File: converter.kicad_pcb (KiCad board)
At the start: 2 copper layers, 26.4 x 49.9 mm, 69 parts, among them CN1 MINI_DIN_8P_JACK, J1 USB_B, J2 USB_microB, SW1 SW_PUSH, U1 ATMEGA32U4, X1 16MHz

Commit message: Initial commit of PCB rev.2
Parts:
- removed 1, 2, 3, 4, 5, 6, 7, 8, AREF, B0, B1, B2, B3, B4, B5, B6, B7, C7, D+, D-, D0, D2, D3, D4, D5, D6, D7, E6, F0, F1, F4, F5, F6, F7, GND (x3), RST, VCC (x2): CONN_1, PIN_1
- removed the C6 at (136.0, 100.3)
- removed the C6 at (148.7, 97.0)
- removed C7, C8: 0.1u, SM0603_Capa
- removed the D1 at (154.9, 97.3)
- removed the D1 at (141.1, 95.2)
- removed the HOLE_M2.6 at (157.2, 124.6)
- removed the HOLE_M2.6 at (137.7, 85.9)
- removed the HOLE_M2.6 at (157.2, 85.9)
- removed the HOLE_M2.6 at (137.7, 124.6)
- removed J2: USB_microB, USB_microB
- removed R5, R6, R7, R8: 1K, SM0603
- added C6: 22p, 000NewKeyboard_parts:C_1608, F.Cu at (122.4, 122.6)
- added D1: LED, 000NewKeyboard_parts:LED_0805, F.Cu at (101.7, 102.9)
- added HOLE_M2.6: VAL**, HOLE_M2.6, F.Cu at (123.0, 134.0)
- added HOLE_M2.6: VAL**, HOLE_M2.6, F.Cu at (103.4, 107.7)
- added HOLE_M2.6: VAL**, HOLE_M2.6, F.Cu at (122.9, 107.7)
- added HOLE_M2.6: VAL**, HOLE_M2.6, F.Cu at (103.5, 134.0)
- added P1: CONN_1, 000NewKeyboard_parts:PIN_1, F.Cu at (116.8, 130.3)
- added P2: CONN_1, 000NewKeyboard_parts:PIN_1, F.Cu at (114.3, 130.3)
- added P3: CONN_1, 000NewKeyboard_parts:PIN_1, F.Cu at (111.7, 130.3)
- added P4: CONN_1, 000NewKeyboard_parts:PIN_1, F.Cu at (109.2, 130.3)
- added R10: 1K, 000NewKeyboard_parts:R_1608, F.Cu at (122.3, 119.7)
- added R11: 1K, 000NewKeyboard_parts:R_1608, F.Cu at (120.7, 117.7)
- added R12: 1K, 000NewKeyboard_parts:R_1608, F.Cu at (122.3, 115.8)
- added R13: 1K, 000NewKeyboard_parts:R_1608, F.Cu at (120.7, 113.8)
- added R14: 1K, 000NewKeyboard_parts:R_1608, F.Cu at (122.3, 111.8)
- added SJ1: SOLDER_JUMPER, 000NewKeyboard_parts:SOLDER_JUMPER_2, B.Cu at (102.6, 112.7)
- added SJ10: SOLDER_JUMPER, 000NewKeyboard_parts:SOLDER_JUMPER_2, B.Cu at (108.6, 118.7)
- added SJ11: SOLDER_JUMPER, 000NewKeyboard_parts:SOLDER_JUMPER_2, B.Cu at (108.6, 121.7)
- added SJ12: SOLDER_JUMPER, 000NewKeyboard_parts:SOLDER_JUMPER_2, B.Cu at (108.6, 124.7)
- added SJ13: SOLDER_JUMPER, 000NewKeyboard_parts:SOLDER_JUMPER_2, B.Cu at (108.6, 127.7)
- added SJ14: SOLDER_JUMPER, 000NewKeyboard_parts:SOLDER_JUMPER_2, B.Cu at (111.6, 115.7)
- added SJ15: SOLDER_JUMPER, 000NewKeyboard_parts:SOLDER_JUMPER_2, B.Cu at (114.6, 112.7)
- added SJ16: SOLDER_JUMPER, 000NewKeyboard_parts:SOLDER_JUMPER_2, B.Cu at (114.6, 115.7)
- added SJ17: SOLDER_JUMPER, 000NewKeyboard_parts:SOLDER_JUMPER_2, B.Cu at (114.6, 118.7)
- added SJ18: SOLDER_JUMPER, 000NewKeyboard_parts:SOLDER_JUMPER_2, B.Cu at (114.6, 121.7)
- added SJ19: SOLDER_JUMPER, 000NewKeyboard_parts:SOLDER_JUMPER_2, B.Cu at (114.6, 124.7)
- added SJ2: SOLDER_JUMPER, 000NewKeyboard_parts:SOLDER_JUMPER_2, B.Cu at (102.6, 115.7)
- added SJ20: SOLDER_JUMPER, 000NewKeyboard_parts:SOLDER_JUMPER_2, B.Cu at (114.6, 127.7)
- added SJ21: SOLDER_JUMPER, 000NewKeyboard_parts:SOLDER_JUMPER_2, B.Cu at (117.6, 112.7)
- added SJ22: SOLDER_JUMPER, 000NewKeyboard_parts:SOLDER_JUMPER_2, B.Cu at (117.6, 121.7)
- added SJ23: SOLDER_JUMPER, 000NewKeyboard_parts:SOLDER_JUMPER_2, B.Cu at (117.6, 124.7)
- added SJ24: SOLDER_JUMPER, 000NewKeyboard_parts:SOLDER_JUMPER_2, B.Cu at (117.6, 127.7)
- added SJ25: SOLDER_JUMPER, 000NewKeyboard_parts:SOLDER_JUMPER_2, B.Cu at (120.6, 112.7)
- added SJ26: SOLDER_JUMPER, 000NewKeyboard_parts:SOLDER_JUMPER_2, B.Cu at (123.6, 112.7)
- added SJ27: SOLDER_JUMPER, 000NewKeyboard_parts:SOLDER_JUMPER_2, B.Cu at (123.6, 115.7)
- added SJ28: SOLDER_JUMPER, 000NewKeyboard_parts:SOLDER_JUMPER_2, B.Cu at (123.6, 118.7)
- added SJ29: SOLDER_JUMPER, 000NewKeyboard_parts:SOLDER_JUMPER_2, B.Cu at (123.6, 124.7)
- added SJ3: SOLDER_JUMPER, 000NewKeyboard_parts:SOLDER_JUMPER_2, B.Cu at (102.6, 118.7)
- added SJ30: SOLDER_JUMPER, 000NewKeyboard_parts:SOLDER_JUMPER_2, B.Cu at (123.6, 127.7)
- added SJ4: SOLDER_JUMPER, 000NewKeyboard_parts:SOLDER_JUMPER_2, B.Cu at (102.6, 121.7)
- added SJ5: SOLDER_JUMPER, 000NewKeyboard_parts:SOLDER_JUMPER_2, B.Cu at (102.6, 124.7)
- added SJ6: SOLDER_JUMPER, 000NewKeyboard_parts:SOLDER_JUMPER_2, B.Cu at (105.6, 112.7)
- added SJ7: SOLDER_JUMPER, 000NewKeyboard_parts:SOLDER_JUMPER_2, B.Cu at (105.6, 115.7)
- added SJ8: SOLDER_JUMPER, 000NewKeyboard_parts:SOLDER_JUMPER_2, B.Cu at (108.6, 112.7)
- added SJ9: SOLDER_JUMPER, 000NewKeyboard_parts:SOLDER_JUMPER_2, B.Cu at (108.6, 115.7)
- added SJ98: SOLDER_JUMPER, 000NewKeyboard_parts:SOLDER_JUMPER_2, F.Cu at (107.1, 133.2)
- added SJ99: SOLDER_JUMPER, 000NewKeyboard_parts:SOLDER_JUMPER_2, F.Cu at (123.5, 103.6)
- C1: footprint SM1206POL -> 000NewKeyboard_parts:C_1608
- C2, C3, C5: footprint SM0603_Capa -> 000NewKeyboard_parts:C_1608
- C4: value 22p -> 0.1u; footprint SM0603_Capa -> 000NewKeyboard_parts:C_1608
- J1: value USB_B -> USB_mini_micro_B; footprint USB_miniB -> 000NewKeyboard_parts:USB_microB
- R1, R2, R3, R4: footprint SM0603 -> 000NewKeyboard_parts:R_1608
- SW1: footprint SW_ALPS_SKSG -> 000NewKeyboard_parts:SW_ALPS_SKRP
- U1: value ATMEGA32U4 -> ATMEGA32U2; footprint TQFP44 -> 000NewKeyboard_parts:QFP32
- X1: footprint FA-238 -> 000NewKeyboard_parts:FA-238
- moved SW1 53.2 mm to (103.8, 128.6), turned to 90 degrees
- moved C5 44.2 mm to (122.4, 129.4)
- moved C4 43.1 mm to (115.9, 122.9), turned to 0 degrees
- moved C2 41.8 mm to (108.3, 126.4)
- moved CN1 40.8 mm to (113.0, 102.8)
- moved X1 40.3 mm to (122.4, 126.0), turned to 0 degrees
- moved C3 40.2 mm to (116.8, 119.1), turned to 0 degrees
- moved U1 39.8 mm to (108.5, 118.7), turned to 180 degrees
- moved R3 39.3 mm to (102.5, 113.5), turned to 180 degrees
- moved R4 38.6 mm to (102.5, 111.3), turned to 0 degrees
- moved J1 36.5 mm to (113.0, 135.6)
- moved R2 36.4 mm to (111.7, 127.0)
- moved R1 32.2 mm to (114.3, 127.0)
- moved C1 26.3 mm to (119.3, 131.2), turned to 270 degrees
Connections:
- C2 pad 1: N-0000022 -> Net-(C2-Pad1)
- C4 pad 1: N-0000037 -> +5V
- C5 pad 1: N-0000038 -> Net-(C5-Pad1)
- CN1 pad 9: (no net) -> Net-(CN1-Pad9)
- J1 pad 4: (no net) -> Net-(J1-Pad4)
- J1 pad 6: (no net) -> Net-(J1-Pad6)
- R1 pad 1: N-0000025 -> Net-(R1-Pad1)
- R2 pad 1: N-0000024 -> Net-(R2-Pad1)
- R3 pad 2: N-0000013 -> /PD7
- R4 pad 1: +5V -> Net-(D1-Pad2)
- R4 pad 2: /PD0 -> GND
- SW1 pad 1: GND -> /~RESET
- SW1 pad 2: /~RESET -> GND
- U1 pad 1: /PE6 -> Net-(C5-Pad1)
- U1 pad 10: /PB2 -> /PD4
- U1 pad 11: /PB3 -> /PD5
- U1 pad 12: /PB7 -> /PD6
- U1 pad 13: /~RESET -> /PD7
- U1 pad 14: +5V -> /PB0
- U1 pad 15: GND -> /PB1
- U1 pad 16: N-0000037 -> /PB2
- U1 pad 17: N-0000038 -> /PB3
- U1 pad 18: /PD0 -> /PB4
- U1 pad 19: /PD1 -> /PB5
- U1 pad 2: +5V -> Net-(C6-Pad1)
- U1 pad 20: /PD2 -> /PB6
- U1 pad 21: /PD3 -> /PB7
- U1 pad 22: /PD5 -> /PC7
- U1 pad 23: GND -> /PC6
- U1 pad 24: +5V -> /~RESET
- U1 pad 25: /PD4 -> /PC5
- U1 pad 26: /PD6 -> /PC4
- U1 pad 27: /PD7 -> Net-(C2-Pad1)
- U1 pad 28: /PB4 -> GND
- U1 pad 29: /PB5 -> Net-(R2-Pad1)
- U1 pad 3: N-0000025 -> GND
- U1 pad 30: /PB6 -> Net-(R1-Pad1)
- U1 pad 31: /PC6 -> +5V
- U1 pad 32: /PC7 -> +5V
- U1 pad 4: N-0000024 -> +5V
- U1 pad 5: GND -> /PC2
- U1 pad 6: N-0000022 -> /PD0
- U1 pad 7: +5V -> /PD1
- U1 pad 8: /PB0 -> /PD2
- U1 pad 9: /PB1 -> /PD3
- X1 pad 1: N-0000037 -> Net-(C5-Pad1)
- X1 pad 2: N-0000038 -> Net-(C6-Pad1)
- X1 pad 3: (no net) -> GND
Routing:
- net GND: track 51.3 -> 151.1 mm, vias 12 -> 4
- net /PD4: track 5.77 -> 33.0 mm, vias 1 -> 2
- net /DIN8: track 7.30 -> 32.9 mm, vias 0 -> 1
- net /DIN5: track 8.30 -> 33.6 mm
- net +5V: track 83.0 -> 104.4 mm, vias 0 -> 4
- net /PD0: track 22.0 -> 43.2 mm, vias 1 -> 5
- net /DIN3: track 8.09 -> 28.9 mm
- net /DIN6: track 9.59 -> 30.0 mm, vias 0 -> 1
- net /PB7: track 19.6 -> 0.00 mm
- net /PD1: track 20.1 -> 39.1 mm, vias 1 -> 3
- net /PB6: track 17.4 -> 0.00 mm, vias 1 -> 0
- net /PE6: track 17.3 -> 0.00 mm, vias 1 -> 0
- net Net-(C6-Pad1): track 0.00 -> 16.8 mm
- net /PB4: track 15.7 -> 0.00 mm, vias 1 -> 0
- net Net-(C5-Pad1): track 0.00 -> 14.8 mm
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- added copper zone on F.Cu, net GND
- removed copper zone on F.Cu, net +5V
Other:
- board size 26.4 x 49.9 mm -> 26 x 37 mm
- net class 12tho removed
- net class Default: trace_width 0.2032 -> 0.254; via_dia 0.762 -> 0.889
- net class Min6mil added: clearance 0.1524, trace_width 0.1524, via_dia 0.889, via_drill 0.508
- net class Min8mil added: clearance 0.2032, trace_width 0.2032, via_dia 0.889, via_drill 0.508
- net class Power added: clearance 0.254, trace_width 0.381, via_dia 0.889, via_drill 0.508
- rule trace_min: 0.2032 -> 0.1524
- board text added: "1"
- board text added: "2"
- board text added: "3"
- board text added: "4"
- board text added: "5"
- board text added: "6"
- board text added: "7"
- board text added: "8"
- board text added: "ADB"
- board text added: "NEXT"
- board text added: "PC98"
- board text added: "PS/2"
- board text added: "SUN"
- board text added: "X68K"
- board text removed: "May 2013"
- board text removed: "TMK"
- board text removed: "Tokyo JAPAN"
- board text removed: "keyboard"
- board text removed: "rev.1"

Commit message: Clean library.
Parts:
- R3: value 1k -> 1K
- U1: value ATMEGA32U2 -> 32U2
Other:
- board text added: "+"
- board text added: "-"
- board text added: "D0"
- board text added: "D1"
- board text added: "D2"
- board text added: "D3"
- board text added: "D4"
- board text added: "FG"
- board text added: "G"
- board text added: "HWB"
- board text added: "V"

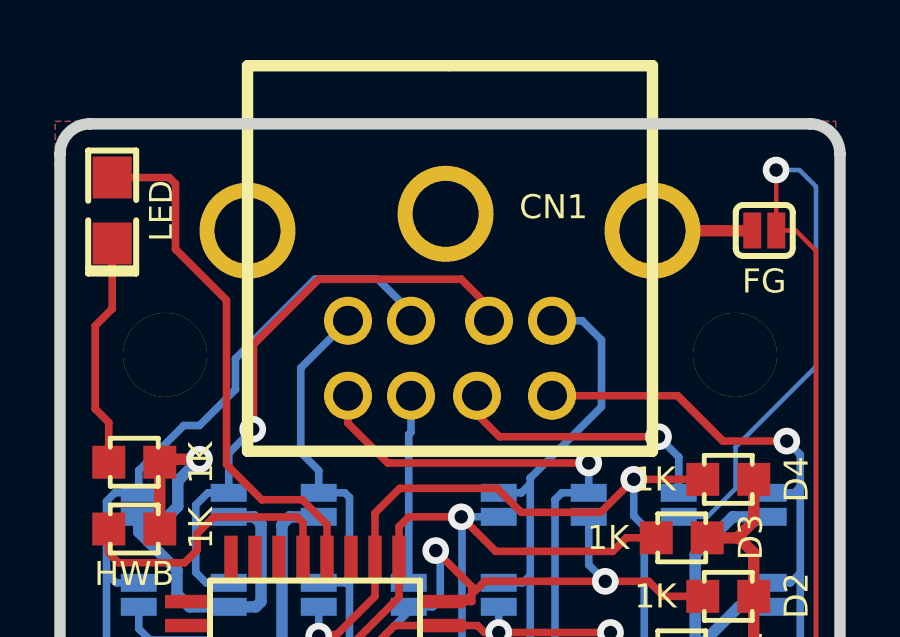
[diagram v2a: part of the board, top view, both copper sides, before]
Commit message: Update Mini DIN module and vix PCB.
- Wrong pad alignment
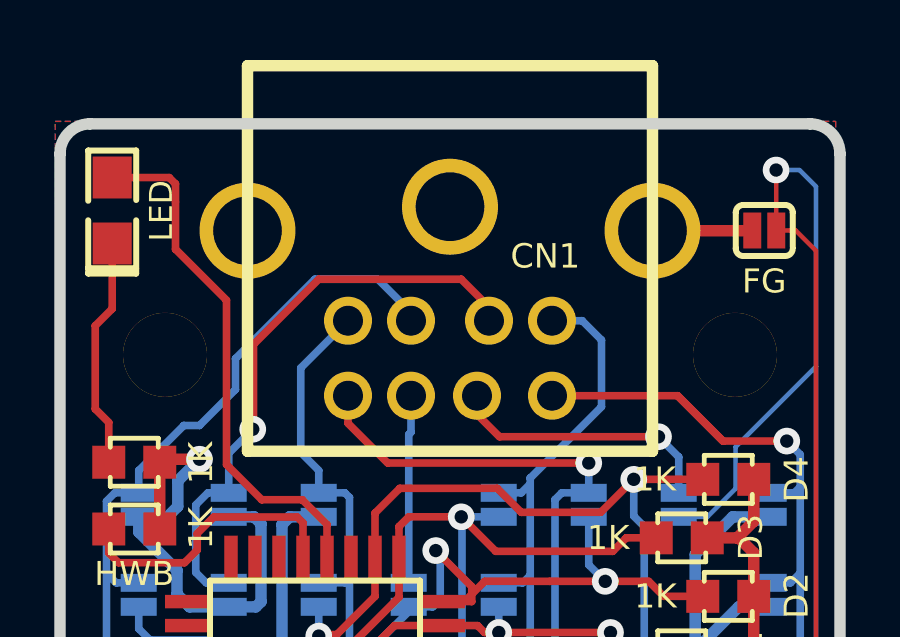
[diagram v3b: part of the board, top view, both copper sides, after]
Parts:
- CN1: footprint MINI_DIN_8 -> 000NewKeyboard_parts:MINI_DIN_8

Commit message: rev2.1
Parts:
- R3: value 1K -> 1k
- R4: value 1K -> R_LED
- U1: value 32U2 -> ATMEGA32U2
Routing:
- net Net-(J1-Pad6): track 4.86 -> 2.43 mm
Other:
- rule pad_to_mask_clearance: 0.254 -> 0.1

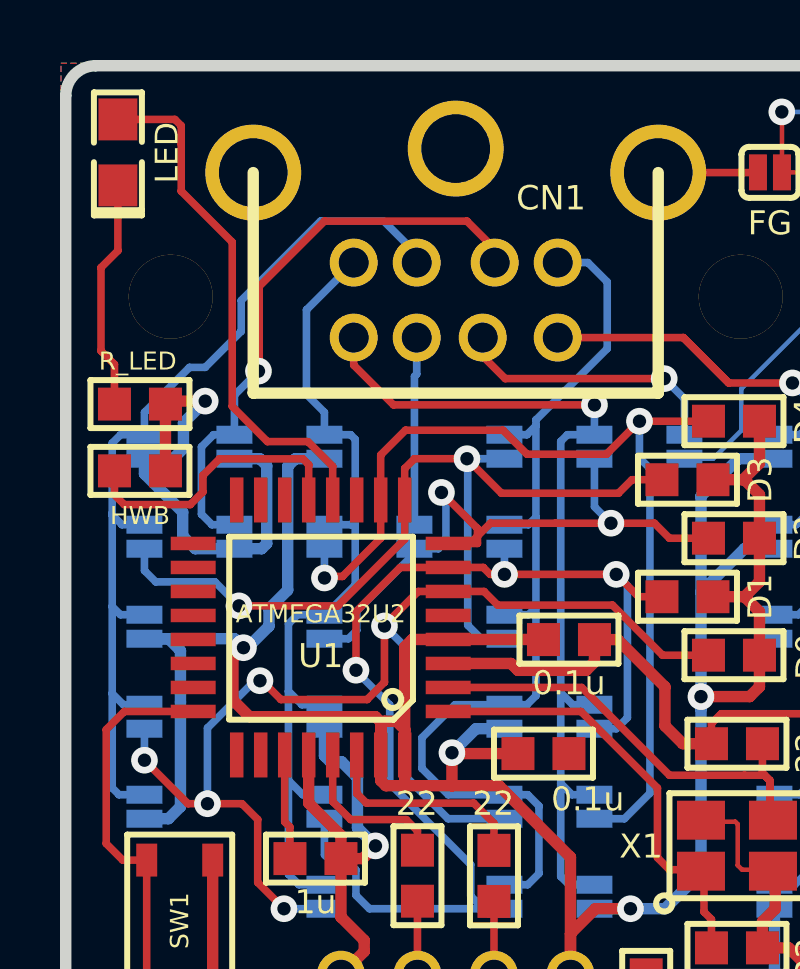
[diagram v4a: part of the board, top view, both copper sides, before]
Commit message: Change LED footprint and add numbering silks
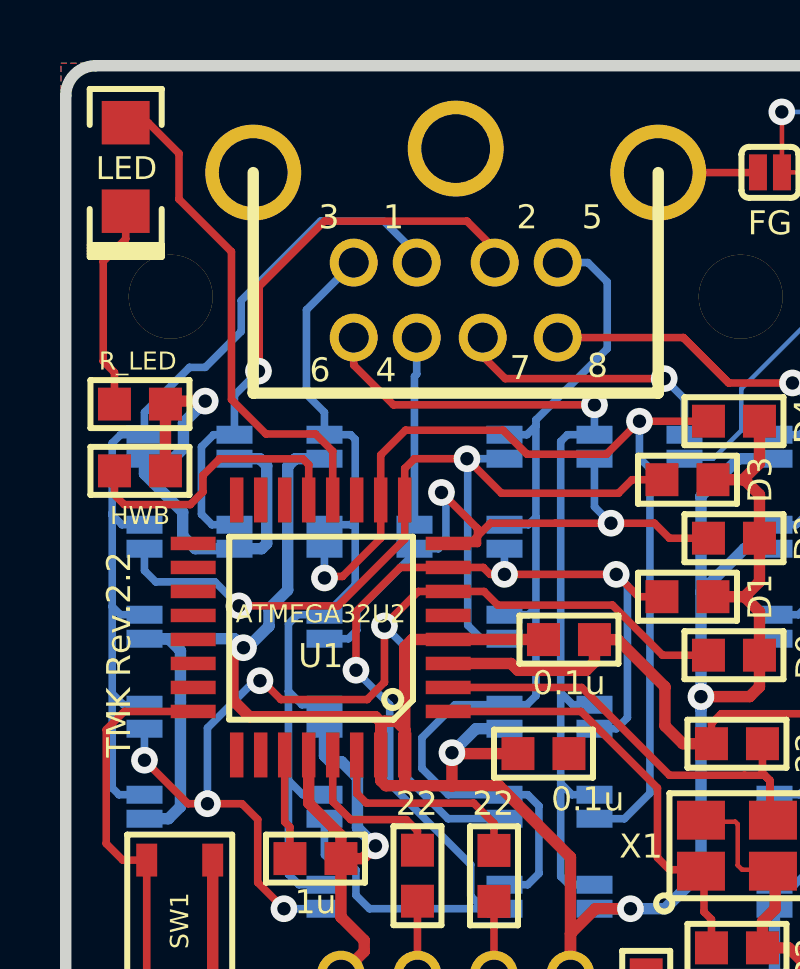
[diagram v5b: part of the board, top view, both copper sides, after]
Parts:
- D1: footprint 000NewKeyboard_parts:LED_0805 -> keyboard_parts:LED_3020_REFLOW
- moved D1 0.55 mm to (102.0, 103.4)
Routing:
- net Net-(D1-Pad2): track 7.71 -> 6.90 mm
- net /PD6: track 17.6 -> 16.8 mm
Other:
- rule pad_to_mask_clearance: 0.1 -> 0.2
- board text added: "TMK Rev.2.2"

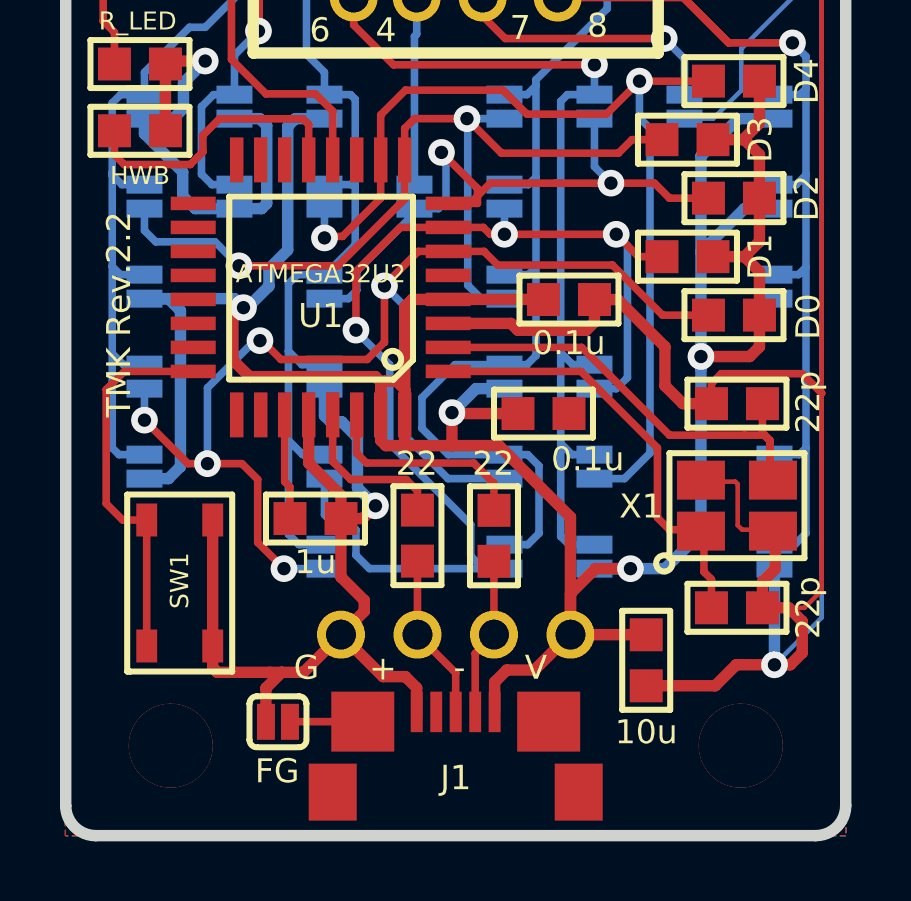
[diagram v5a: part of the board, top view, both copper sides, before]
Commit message: Change values of capacitors and solder mask setting
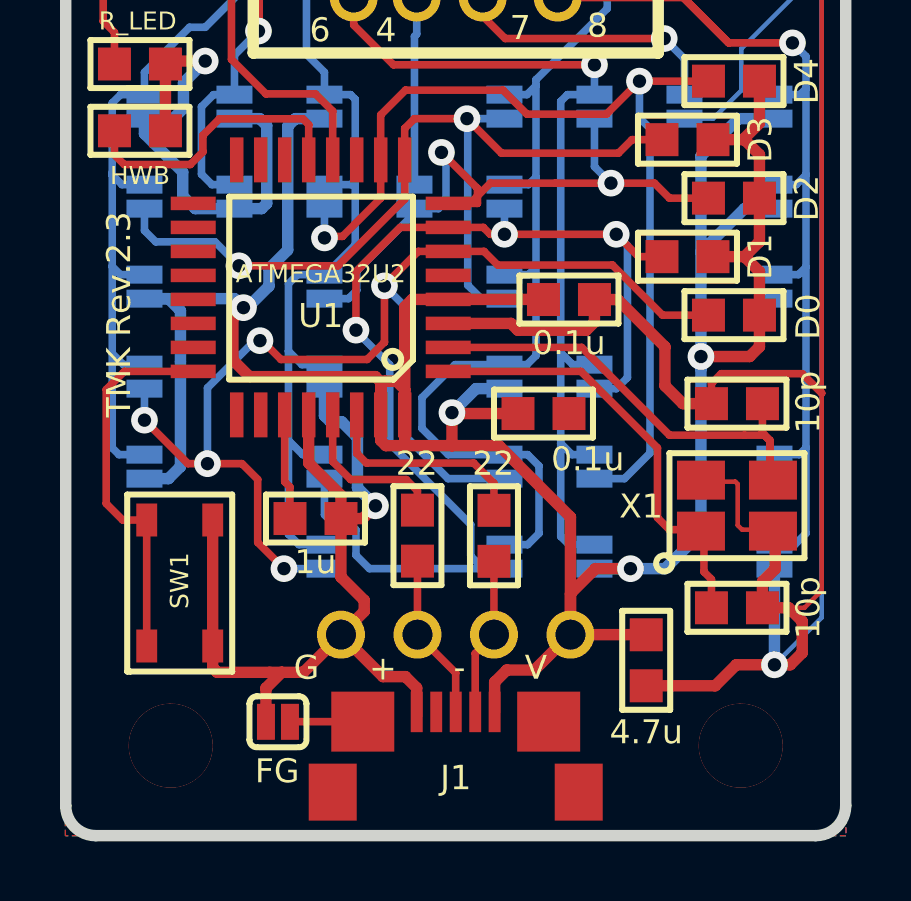
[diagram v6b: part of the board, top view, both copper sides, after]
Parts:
- C1: value 10u -> 4.7u
- C5, C6: value 22p -> 10p
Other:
- rule pad_to_mask_clearance: 0.2 -> 0.075
- rule solder_mask_min_width: 0.2 -> 0.15
- board text added: "TMK Rev.2.3"
- board text removed: "TMK Rev.2.2"
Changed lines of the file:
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@@
   (title_block
     (title "Keyboard Protocol Converter")
-    (rev 1)
+    (date 2015/12)
+    (rev 2.3)
     (company TMK)
   )
@@
     (pad_size 1.6 1.9)
     (pad_drill 0)
-    (pad_to_mask_clearance 0.2)
-    (solder_mask_min_width 0.2)
+    (pad_to_mask_clearance 0.075)
+    (solder_mask_min_width 0.15)
     (pad_to_paste_clearance -0.08)
     (aux_axis_origin 100 100)
@@
       (drillshape 0)
       (scaleselection 1)
-      (outputdirectory plot/rev2_2/))
+      (outputdirectory plot/rev2_3/))
   )
   (net 0 "")
@@
       (effects (font (size 0.8 0.8) (thickness 0.15)))
     )
-    (fp_text value 10u (at 2.395 0 360) (layer F.SilkS)
+    (fp_text value 4.7u (at 2.395 0 360) (layer F.SilkS)
       (effects (font (size 0.8 0.8) (thickness 0.15)))
     )
@@
       (effects (font (size 0.8 0.8) (thickness 0.15)))
     )
-    (fp_text value 22p (at -2.375 0.05 270) (layer F.SilkS)
+    (fp_text value 10p (at -2.375 0.05 270) (layer F.SilkS)
       (effects (font (size 0.8 0.8) (thickness 0.15)))
     )
@@
       (effects (font (size 0.8 0.8) (thickness 0.15)))
     )
-    (fp_text value 22p (at 2.375 -0.005 90) (layer F.SilkS)
+    (fp_text value 10p (at 2.375 -0.005 90) (layer F.SilkS)
       (effects (font (size 0.8 0.8) (thickness 0.15)))
     )
@@
       (net 35 "Net-(D1-Pad2)"))
   )
-  (gr_text "TMK Rev.2.2" (at 101.775 119.625 90) (layer F.SilkS)
+  (gr_text "TMK Rev.2.3" (at 101.775 119.625 90) (layer F.SilkS)
     (effects (font (size 0.8 0.8) (thickness 0.15)))
   )
